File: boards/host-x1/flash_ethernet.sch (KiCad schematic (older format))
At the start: 81 parts, among them J4 BEL_FUSE_0826-1G1T-23-F, Q1 SSM6N58NU, Q2 SSM6N58NU, Q3 SSM6N58NU, Q4 SSM6N58NU, U10 DSC6102CI2A-100.0000, U11 S25FS064S_BGA, U2 XC7A100T-1FTG256C, U8 KSZ9031RN, U9 DSC6101CI2A-025.0000

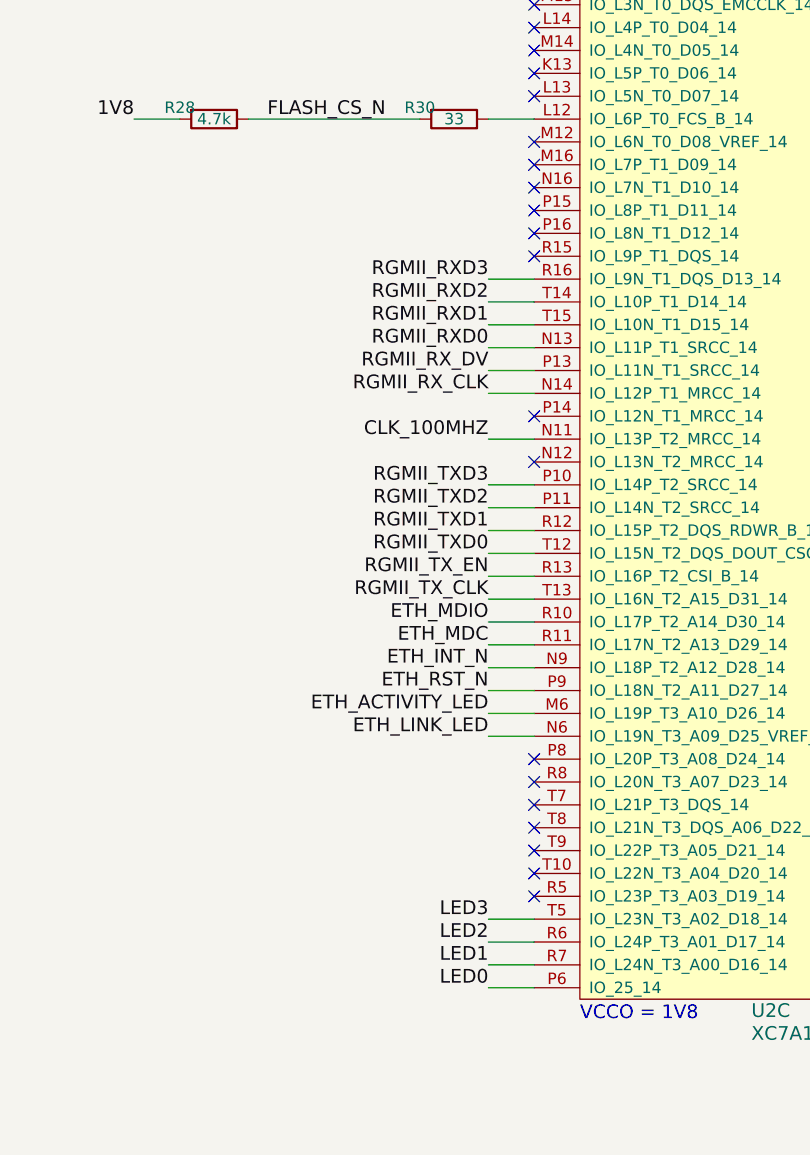
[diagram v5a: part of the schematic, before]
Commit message: Continued layout. Lots of decoupling, partial work on expansion connector, various slow stuff like LEDs
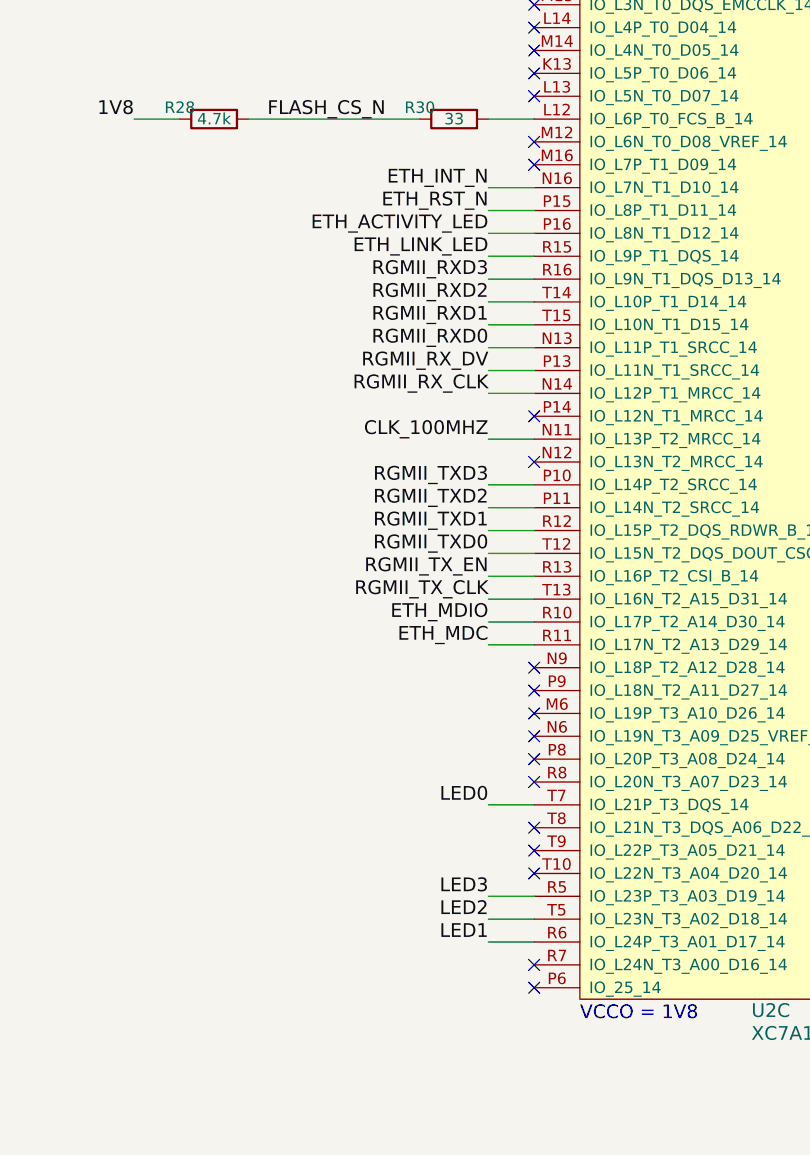
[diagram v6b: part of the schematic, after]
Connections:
- net ETH_ACTIVITY_LED: now also U2.P16 (IO_L8N_T1_D12_14); no longer U2.M6 (IO_L19P_T3_A10_D26_14)
- net ETH_INT_N: now also U2.N16 (IO_L7N_T1_D10_14); no longer U2.N9 (IO_L18P_T2_A12_D28_14)
- net ETH_LINK_LED: now also U2.R15 (IO_L9P_T1_DQS_14); no longer U2.N6 (IO_L19N_T3_A09_D25_VREF_14)
- net ETH_RST_N: now also U2.P15 (IO_L8P_T1_D11_14); no longer U2.P9 (IO_L18N_T2_A11_D27_14)
- net LED0: now also U2.T7 (IO_L21P_T3_DQS_14); no longer U2.P6 (IO_25_14)
- net LED1: now also U2.R6 (IO_L24P_T3_A01_D17_14); no longer U2.R7 (IO_L24N_T3_A00_D16_14)
- net LED2: now also U2.T5 (IO_L23N_T3_A02_D18_14); no longer U2.R6 (IO_L24P_T3_A01_D17_14)
- net LED3: now also U2.R5 (IO_L23P_T3_A03_D19_14); no longer U2.T5 (IO_L23N_T3_A02_D18_14)
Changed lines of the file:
@@
 $EndDescr
-$Comp
-L XC7AxT-xFTG256x U?
-U 3 1 590E87C3
-P 14200 5750
-AR Path="/590BFAB4/590E87C3" Ref="U?"  Part="6"
-AR Path="/590BFAE6/590E87C3" Ref="U?"  Part="3"
-AR Path="/590E8635/590E87C3" Ref="U2"  Part="3"
-F 0 "U2" H 14950 5650 60  0000 L CNN
-F 1 "XC7A100T-1FTG256C" H 14950 5550 60  0000 L CNN
-F 2 "azonenberg_pcb:BGA_256_17x17_FULLARRAY_1MM" H 14200 5750 60  0001 C CNN
-F 3 "" H 14200 5750 60  0000 C CNN
-	3    14200 5750
-	1    0    0    -1
-$EndComp
 $Comp
 L R R29
@@
 	0    -1   -1   0
 $EndComp
-Text Label 13800 5750 2    60   ~ 0
+Text Label 13800 4950 2    60   ~ 0
 LED0
-Text Label 13800 5650 2    60   ~ 0
+Text Label 13800 5550 2    60   ~ 0
 LED1
-Text Label 13800 5550 2    60   ~ 0
+Text Label 13800 5450 2    60   ~ 0
 LED2
-Text Label 13800 5450 2    60   ~ 0
+Text Label 13800 5350 2    60   ~ 0
 LED3
 Text Label 13800 3550 2    60   ~ 0
@@
 	0    1    1    0
 $EndComp
-Text Label 13800 4350 2    60   ~ 0
+Text Label 13800 2250 2    60   ~ 0
 ETH_INT_N
 Text Label 8100 3250 0    60   ~ 0
 ETH_RST_N
-Text Label 13800 4450 2    60   ~ 0
+Text Label 13800 2350 2    60   ~ 0
 ETH_RST_N
 NoConn ~ 14000 3450
@@
 NoConn ~ 14000 1850
 NoConn ~ 14000 2050
-NoConn ~ 14000 2350
-NoConn ~ 14000 2450
-NoConn ~ 14000 2550
 NoConn ~ 14000 4750
 NoConn ~ 14000 4850
-NoConn ~ 14000 4950
 NoConn ~ 14000 5050
 NoConn ~ 14000 5150
 NoConn ~ 14000 5250
-NoConn ~ 14000 5350
 Wire Wire Line
 	13800 1350 14000 1350
@@
 Connection ~ 4100 10300
 Wire Wire Line
-	13800 5750 14000 5750
-Wire Wire Line
-	14000 5650 13800 5650
-Wire Wire Line
-	13800 5550 14000 5550
+	13800 4950 14000 4950
+Wire Wire Line
+	14000 5550 13800 5550
+Wire Wire Line
+	13800 5350 14000 5350
 Wire Wire Line
 	13800 5450 14000 5450
@@
 	8100 3050 7900 3050
 Wire Wire Line
-	13800 4350 14000 4350
+	13800 2250 14000 2250
 Wire Wire Line
 	8100 3250 7300 3250
 Wire Wire Line
-	13800 4450 14000 4450
+	13800 2350 14000 2350
 Wire Wire Line
 	13800 3350 14000 3350
@@
 Wire Wire Line
 	8100 3150 7900 3150
-NoConn ~ 14000 2250
 NoConn ~ 14000 2150
 $Comp
@@
 Connection ~ 5350 10300
 Connection ~ 7250 10300
-Text Label 13800 4550 2    60   ~ 0
+Text Label 13800 2450 2    60   ~ 0
 ETH_ACTIVITY_LED
-Text Label 13800 4650 2    60   ~ 0
+Text Label 13800 2550 2    60   ~ 0
 ETH_LINK_LED
 Wire Wire Line
-	13800 4550 14000 4550
-Wire Wire Line
-	14000 4650 13800 4650
+	13800 2450 14000 2450
+Wire Wire Line
+	14000 2550 13800 2550
 $Comp
 L S25FS064S_BGA U11
@@
 Text Notes 8950 10950 0    60   ~ 0
 Tie off unused transistor
+NoConn ~ 14000 5650
+NoConn ~ 14000 5750
+NoConn ~ 14000 4650
+NoConn ~ 14000 4550
+$Comp
+L XC7AxT-xFTG256x U?
+U 3 1 590E87C3
+P 14200 5750
+AR Path="/590BFAB4/590E87C3" Ref="U?"  Part="6"
+AR Path="/590BFAE6/590E87C3" Ref="U?"  Part="3"
+AR Path="/590E8635/590E87C3" Ref="U2"  Part="3"
+F 0 "U2" H 14950 5650 60  0000 L CNN
+F 1 "XC7A100T-1FTG256C" H 14950 5550 60  0000 L CNN
+F 2 "azonenberg_pcb:BGA_256_17x17_FULLARRAY_1MM" H 14200 5750 60  0001 C CNN
+F 3 "" H 14200 5750 60  0000 C CNN
+	3    14200 5750
+	1    0    0    -1
+$EndComp
+NoConn ~ 14000 4450
+NoConn ~ 14000 4350
 $EndSCHEMATC

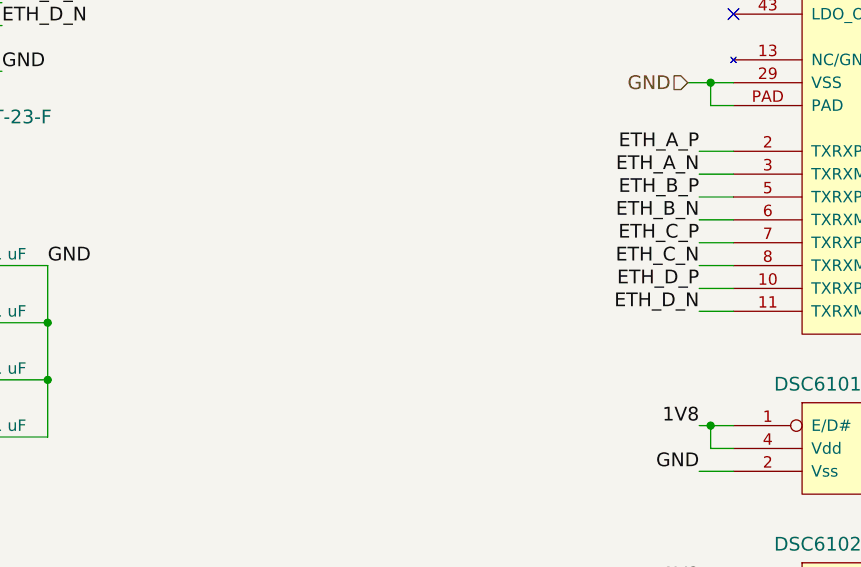
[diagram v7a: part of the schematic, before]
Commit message: Began routing Ethernet. Lots of tweaks to power plane layout.
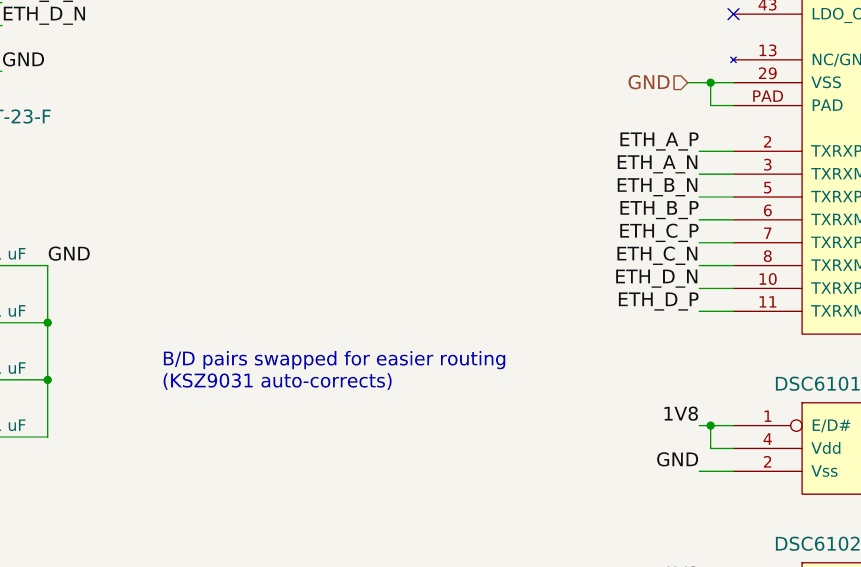
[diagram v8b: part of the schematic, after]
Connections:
- net ETH_B_N: now also U8.5 (TXRXP_B); no longer U8.6 (TXRXM_B)
- net ETH_B_P: now also U8.6 (TXRXM_B); no longer U8.5 (TXRXP_B)
- net ETH_D_N: now also U8.10 (TXRXP_D); no longer U8.11 (TXRXM_D)
- net ETH_D_P: now also U8.11 (TXRXM_D); no longer U8.10 (TXRXP_D)
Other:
- note added: "B/D pairs swapped for easier routing\n(KSZ9031 auto-corrects)"
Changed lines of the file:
@@
 Text Label 4900 3450 2    60   ~ 0
 ETH_A_N
+Text Label 4900 3650 2    60   ~ 0
+ETH_B_P
 Text Label 4900 3550 2    60   ~ 0
-ETH_B_P
-Text Label 4900 3650 2    60   ~ 0
 ETH_B_N
 Text Label 4900 3750 2    60   ~ 0
@@
 Text Label 4900 3850 2    60   ~ 0
 ETH_C_N
+Text Label 4900 4050 2    60   ~ 0
+ETH_D_P
 Text Label 4900 3950 2    60   ~ 0
-ETH_D_P
-Text Label 4900 4050 2    60   ~ 0
 ETH_D_N
 $Comp
@@
 NoConn ~ 14000 4450
 NoConn ~ 14000 4350
+Text Notes 2550 4400 0    60   ~ 0
+B/D pairs swapped for easier routing\n(KSZ9031 auto-corrects)
 $EndSCHEMATC
